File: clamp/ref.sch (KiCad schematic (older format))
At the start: 23 parts, among them P4 CONN_01X06, Q1 2N3904, U12 LTZ1000, U13 LM741, U14 LM741

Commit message: add extra caps, and separate heater gnd return
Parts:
- removed P4: CONN_01X06, Pin_Headers:Pin_Header_Straight_1x06, symbol CONN_01X06
- added C31, C32: C, Capacitors_SMD:C_1206, symbol C
- added P4: CONN_01X08, symbol CONN_01X08
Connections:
- net +VE: now also C31.1, P4.1 (P1)
- net -VE: now also C32.1, P4.3 (P3)
- net GND: now also C31.2, C32.2, P4.2 (P2), P4.6 (P6), P4.7 (P7), P4.8 (P8); no longer D8.2 (C)
- net REF: now also P4.4 (P4)
- new net GND-H: D8.2 (C), P4.5 (P5)
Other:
- moved on the sheet: C27, C28, C33, C34
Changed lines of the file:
@@
 REF
 Connection ~ 9250 2250
-$Comp
-L CONN_01X06 P4
-U 1 1 58643775
-P 2900 1300
-F 0 "P4" H 2900 1650 50  0000 C CNN
-F 1 "CONN_01X06" V 3000 1300 50  0000 C CNN
-F 2 "Pin_Headers:Pin_Header_Straight_1x06" H 2900 1300 50  0001 C CNN
-F 3 "" H 2900 1300 50  0000 C CNN
-	1    2900 1300
-	-1   0    0    -1
-$EndComp
-Text GLabel 3100 1050 2    60   Input ~ 0
+Text GLabel 2850 900  2    60   Input ~ 0
 +VE
-Text GLabel 3100 1250 2    60   Input ~ 0
+Text GLabel 2850 1100 2    60   Input ~ 0
 -VE
-Text GLabel 3100 1150 2    60   Input ~ 0
-GND
-Text GLabel 3100 1350 2    60   Input ~ 0
+Text GLabel 2850 1000 2    60   Input ~ 0
+GND
+Text GLabel 2850 1200 2    60   Input ~ 0
 REF
-Text GLabel 3100 1450 2    60   Input ~ 0
-GND
-Text GLabel 3100 1550 2    60   Input ~ 0
+Text GLabel 2850 1600 2    60   Input ~ 0
+GND
+Text GLabel 2850 1400 2    60   Input ~ 0
 GND
 NoConn ~ 8350 3450
@@
 L C C27
 U 1 1 586449E6
-P 6550 1100
-F 0 "C27" H 6575 1200 50  0000 L CNN
-F 1 "C" H 6575 1000 50  0000 L CNN
-F 2 "Capacitors_SMD:C_1206" H 6588 950 50  0001 C CNN
-F 3 "" H 6550 1100 50  0000 C CNN
-	1    6550 1100
-	1    0    0    -1
-$EndComp
-Text GLabel 6350 850  1    60   Input ~ 0
+P 4700 1100
+F 0 "C27" H 4725 1200 50  0000 L CNN
+F 1 "C" H 4725 1000 50  0000 L CNN
+F 2 "Capacitors_SMD:C_1206" H 4738 950 50  0001 C CNN
+F 3 "" H 4700 1100 50  0000 C CNN
+	1    4700 1100
+	1    0    0    -1
+$EndComp
+Text GLabel 4500 850  1    60   Input ~ 0
 +VE
 Wire Wire Line
-	6350 850  6350 950
-Wire Wire Line
-	6350 950  6800 950
-Connection ~ 6550 950
-Text GLabel 6550 1250 3    60   Input ~ 0
+	4500 850  4500 950
+Wire Wire Line
+	4500 950  5200 950
+Connection ~ 4700 950
+Text GLabel 4700 1250 3    60   Input ~ 0
 GND
 $Comp
 L C C28
 U 1 1 586449F9
-P 6800 1100
-F 0 "C28" H 6825 1200 50  0000 L CNN
-F 1 "C" H 6825 1000 50  0000 L CNN
-F 2 "Capacitors_SMD:C_1206" H 6838 950 50  0001 C CNN
-F 3 "" H 6800 1100 50  0000 C CNN
-	1    6800 1100
-	1    0    0    -1
-$EndComp
-Connection ~ 6800 950
-Text GLabel 6800 1250 3    60   Input ~ 0
+P 4950 1100
+F 0 "C28" H 4975 1200 50  0000 L CNN
+F 1 "C" H 4975 1000 50  0000 L CNN
+F 2 "Capacitors_SMD:C_1206" H 4988 950 50  0001 C CNN
+F 3 "" H 4950 1100 50  0000 C CNN
+	1    4950 1100
+	1    0    0    -1
+$EndComp
+Connection ~ 4950 950
+Text GLabel 4950 1250 3    60   Input ~ 0
 GND
 $Comp
 L C C33
 U 1 1 58644A04
-P 8500 1100
-F 0 "C33" H 8525 1200 50  0000 L CNN
-F 1 "C" H 8525 1000 50  0000 L CNN
-F 2 "Capacitors_SMD:C_1206" H 8538 950 50  0001 C CNN
-F 3 "" H 8500 1100 50  0000 C CNN
-	1    8500 1100
-	1    0    0    -1
-$EndComp
-Wire Wire Line
-	8300 850  8300 950
-Wire Wire Line
-	8300 950  8750 950
-Connection ~ 8500 950
-Text GLabel 8500 1250 3    60   Input ~ 0
+P 6650 1100
+F 0 "C33" H 6675 1200 50  0000 L CNN
+F 1 "C" H 6675 1000 50  0000 L CNN
+F 2 "Capacitors_SMD:C_1206" H 6688 950 50  0001 C CNN
+F 3 "" H 6650 1100 50  0000 C CNN
+	1    6650 1100
+	1    0    0    -1
+$EndComp
+Wire Wire Line
+	6450 850  6450 950
+Wire Wire Line
+	6450 950  7150 950
+Connection ~ 6650 950
+Text GLabel 6650 1250 3    60   Input ~ 0
 GND
 $Comp
 L C C34
 U 1 1 58644A16
-P 8750 1100
-F 0 "C34" H 8775 1200 50  0000 L CNN
-F 1 "C" H 8775 1000 50  0000 L CNN
-F 2 "Capacitors_SMD:C_1206" H 8788 950 50  0001 C CNN
-F 3 "" H 8750 1100 50  0000 C CNN
-	1    8750 1100
-	1    0    0    -1
-$EndComp
-Connection ~ 8750 950
-Text GLabel 8750 1250 3    60   Input ~ 0
-GND
-Text GLabel 8300 850  1    60   Input ~ 0
+P 6900 1100
+F 0 "C34" H 6925 1200 50  0000 L CNN
+F 1 "C" H 6925 1000 50  0000 L CNN
+F 2 "Capacitors_SMD:C_1206" H 6938 950 50  0001 C CNN
+F 3 "" H 6900 1100 50  0000 C CNN
+	1    6900 1100
+	1    0    0    -1
+$EndComp
+Connection ~ 6900 950
+Text GLabel 6900 1250 3    60   Input ~ 0
+GND
+Text GLabel 6450 850  1    60   Input ~ 0
 -VE
 Wire Wire Line
@@
 Connection ~ 4300 4200
 Wire Wire Line
-	5050 3750 5050 4200
-Connection ~ 5050 4200
+	5050 3750 5050 4450
+Text GLabel 5050 4450 3    60   Input ~ 0
+GND-H
+Text GLabel 2850 1300 2    60   Input ~ 0
+GND-H
+$Comp
+L CONN_01X08 P4
+U 1 1 586C60C9
+P 2650 1250
+F 0 "P4" H 2650 1700 50  0000 C CNN
+F 1 "CONN_01X08" V 2750 1250 50  0000 C CNN
+F 2 "" H 2650 1250 50  0000 C CNN
+F 3 "" H 2650 1250 50  0000 C CNN
+	1    2650 1250
+	-1   0    0    -1
+$EndComp
+Text GLabel 2850 1500 2    60   Input ~ 0
+GND
+$Comp
+L C C31
+U 1 1 586C63F8
+P 5200 1100
+F 0 "C31" H 5225 1200 50  0000 L CNN
+F 1 "C" H 5225 1000 50  0000 L CNN
+F 2 "Capacitors_SMD:C_1206" H 5238 950 50  0001 C CNN
+F 3 "" H 5200 1100 50  0000 C CNN
+	1    5200 1100
+	1    0    0    -1
+$EndComp
+Text GLabel 5200 1250 3    60   Input ~ 0
+GND
+$Comp
+L C C32
+U 1 1 586C6539
+P 7150 1100
+F 0 "C32" H 7175 1200 50  0000 L CNN
+F 1 "C" H 7175 1000 50  0000 L CNN
+F 2 "Capacitors_SMD:C_1206" H 7188 950 50  0001 C CNN
+F 3 "" H 7150 1100 50  0000 C CNN
+	1    7150 1100
+	1    0    0    -1
+$EndComp
+Text GLabel 7150 1250 3    60   Input ~ 0
+GND
 $EndSCHEMATC

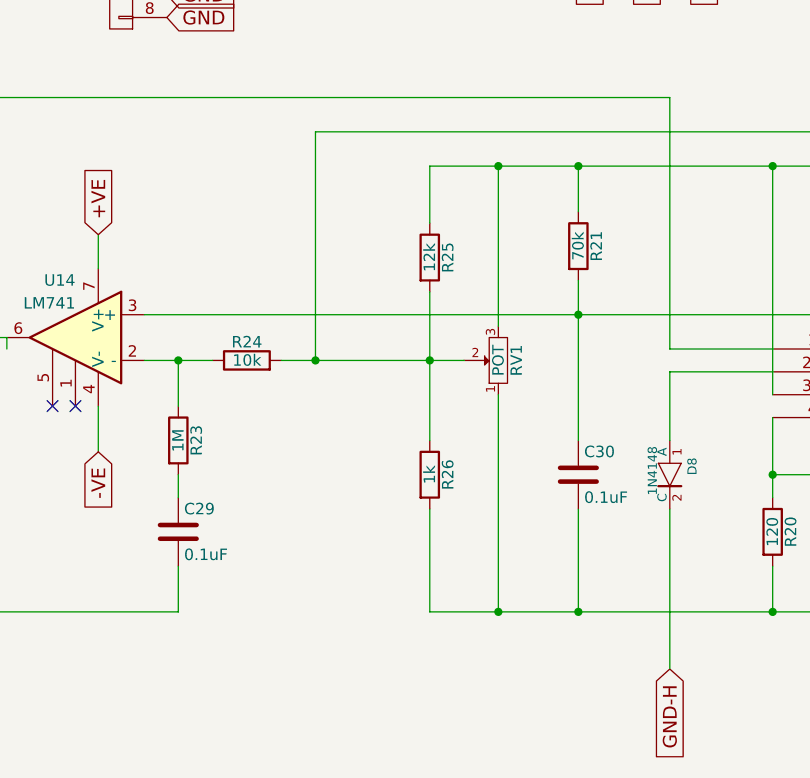
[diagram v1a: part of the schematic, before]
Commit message: remove trimpot add extra resitor
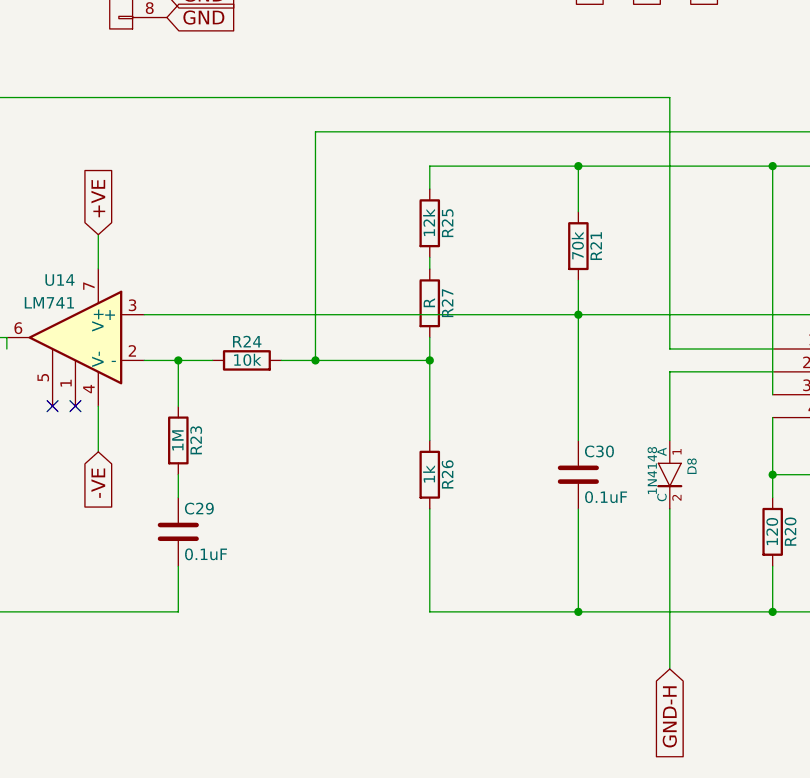
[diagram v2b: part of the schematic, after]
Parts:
- removed RV1: POT, Potentiometers:Potentiometer_Bourns_3296Y_3-8Zoll_Angular_ScrewUp, symbol POT
- added R27: R, symbol R
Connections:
- net at R24.2, R26.1, U12.6 (B2): now also R27.2; no longer R25.2
- new net: R25.2, R27.1
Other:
- moved on the sheet: R25
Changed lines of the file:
@@
 	-1   0    0    -1
 $EndComp
-$Comp
-L POT RV1
-U 1 1 5864A545
-P 4300 3100
-F 0 "RV1" H 4300 3020 50  0000 C CNN
-F 1 "POT" H 4300 3100 50  0000 C CNN
-F 2 "Potentiometers:Potentiometer_Bourns_3296Y_3-8Zoll_Angular_ScrewUp" H 4300 3100 50  0001 C CNN
-F 3 "" H 4300 3100 50  0000 C CNN
-	1    4300 3100
-	0    -1   -1   0
-$EndComp
 Connection ~ 5500 2250
 Wire Wire Line
 	2750 2900 6600 2900
-Wire Wire Line
-	4300 2250 4300 2950
-Wire Wire Line
-	4300 3250 4300 4200
 Connection ~ 5500 4200
 Wire Wire Line
@@
 	2750 3100 3050 3100
 Wire Wire Line
-	3350 3100 4150 3100
+	3350 3100 4000 3100
 Wire Wire Line
 	5050 3150 5500 3150
@@
 L R R25
 U 1 1 5865B477
-P 4000 2650
-F 0 "R25" V 4080 2650 50  0000 C CNN
-F 1 "12k" V 4000 2650 50  0000 C CNN
-F 2 "Resistors_ThroughHole:Resistor_TO-220_Vertical" V 3930 2650 50  0001 C CNN
-F 3 "" H 4000 2650 50  0000 C CNN
-	1    4000 2650
+P 4000 2500
+F 0 "R25" V 4080 2500 50  0000 C CNN
+F 1 "12k" V 4000 2500 50  0000 C CNN
+F 2 "Resistors_ThroughHole:Resistor_TO-220_Vertical" V 3930 2500 50  0001 C CNN
+F 3 "" H 4000 2500 50  0000 C CNN
+	1    4000 2500
 	1    0    0    -1
 $EndComp
@@
 $EndComp
 Wire Wire Line
-	4000 2250 4000 2500
-Connection ~ 4300 2250
-Wire Wire Line
-	4000 2800 4000 3450
+	4000 3000 4000 3450
 Connection ~ 4000 3100
 Wire Wire Line
 	4000 3750 4000 4200
-Connection ~ 4300 4200
 Wire Wire Line
 	5050 3750 5050 4450
@@
 Text GLabel 7150 1250 3    60   Input ~ 0
 GND
+$Comp
+L R R27
+U 1 1 586C6B33
+P 4000 2850
+F 0 "R27" V 4080 2850 50  0000 C CNN
+F 1 "R" V 4000 2850 50  0000 C CNN
+F 2 "" V 3930 2850 50  0000 C CNN
+F 3 "" H 4000 2850 50  0000 C CNN
+	1    4000 2850
+	1    0    0    -1
+$EndComp
+Wire Wire Line
+	4000 2650 4000 2700
+Wire Wire Line
+	4000 2250 4000 2350
 $EndSCHEMATC

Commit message: update
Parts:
- added R28: 0, symbol R
- C27, C33: value C -> 10uF
- C28, C31, C32, C34: value C -> 0.1uF
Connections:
- net GND: now also R28.1
- net GND-H: now also R28.2
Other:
- moved on the sheet: C26, R20, r1
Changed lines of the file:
@@
 L R R20
 U 1 1 58642F48
-P 5500 3850
-F 0 "R20" V 5580 3850 50  0000 C CNN
-F 1 "120" V 5500 3850 50  0000 C CNN
-F 2 "Resistors_ThroughHole:Resistor_TO-220_Vertical" V 5430 3850 50  0001 C CNN
-F 3 "" H 5500 3850 50  0000 C CNN
-	1    5500 3850
-	1    0    0    -1
-$EndComp
-Wire Wire Line
-	5500 3350 5500 3700
+P 5500 3900
+F 0 "R20" V 5580 3900 50  0000 C CNN
+F 1 "120" V 5500 3900 50  0000 C CNN
+F 2 "Resistors_ThroughHole:Resistor_TO-220_Vertical" V 5430 3900 50  0001 C CNN
+F 3 "" H 5500 3900 50  0000 C CNN
+	1    5500 3900
+	1    0    0    -1
+$EndComp
+Wire Wire Line
+	5500 3350 5500 3750
 $Comp
 L R r1
 U 1 1 5864309C
-P 7400 2600
-F 0 "r1" V 7480 2600 50  0000 C CNN
-F 1 "70k" V 7400 2600 50  0000 C CNN
-F 2 "Resistors_ThroughHole:Resistor_TO-220_Vertical" V 7330 2600 50  0001 C CNN
-F 3 "" H 7400 2600 50  0000 C CNN
-	1    7400 2600
-	1    0    0    -1
-$EndComp
-Wire Wire Line
-	7400 2250 7400 2450
+P 7400 2650
+F 0 "r1" V 7480 2650 50  0000 C CNN
+F 1 "70k" V 7400 2650 50  0000 C CNN
+F 2 "Resistors_ThroughHole:Resistor_TO-220_Vertical" V 7330 2650 50  0001 C CNN
+F 3 "" H 7400 2650 50  0000 C CNN
+	1    7400 2650
+	1    0    0    -1
+$EndComp
+Wire Wire Line
+	7400 2250 7400 2500
 Connection ~ 7400 2250
 Wire Wire Line
-	7400 2750 7400 3700
+	7400 2800 7400 3750
 Wire Wire Line
 	6500 3250 6800 3250
@@
 Connection ~ 5500 3600
 Wire Wire Line
-	5500 4200 5500 4000
+	5500 4200 5500 4050
 $Comp
 L C C26
 U 1 1 58643272
-P 7400 3850
-F 0 "C26" H 7425 3950 50  0000 L CNN
-F 1 "22nF" H 7425 3750 50  0000 L CNN
-F 2 "Capacitors_SMD:C_1206" H 7438 3700 50  0001 C CNN
-F 3 "" H 7400 3850 50  0000 C CNN
-	1    7400 3850
-	1    0    0    -1
-$EndComp
-Wire Wire Line
-	7400 4000 7400 4450
+P 7400 3900
+F 0 "C26" H 7425 4000 50  0000 L CNN
+F 1 "22nF" H 7425 3800 50  0000 L CNN
+F 2 "Capacitors_SMD:C_1206" H 7438 3750 50  0001 C CNN
+F 3 "" H 7400 3900 50  0000 C CNN
+	1    7400 3900
+	1    0    0    -1
+$EndComp
+Wire Wire Line
+	7400 4050 7400 4450
 Connection ~ 7400 4200
 Wire Wire Line
@@
 P 4700 1100
 F 0 "C27" H 4725 1200 50  0000 L CNN
-F 1 "C" H 4725 1000 50  0000 L CNN
+F 1 "10uF" H 4725 1000 50  0000 L CNN
 F 2 "Capacitors_SMD:C_1206" H 4738 950 50  0001 C CNN
 F 3 "" H 4700 1100 50  0000 C CNN
@@
 P 4950 1100
 F 0 "C28" H 4975 1200 50  0000 L CNN
-F 1 "C" H 4975 1000 50  0000 L CNN
+F 1 "0.1uF" H 4975 1000 50  0000 L CNN
 F 2 "Capacitors_SMD:C_1206" H 4988 950 50  0001 C CNN
 F 3 "" H 4950 1100 50  0000 C CNN
@@
 P 6650 1100
 F 0 "C33" H 6675 1200 50  0000 L CNN
-F 1 "C" H 6675 1000 50  0000 L CNN
+F 1 "10uF" H 6675 1000 50  0000 L CNN
 F 2 "Capacitors_SMD:C_1206" H 6688 950 50  0001 C CNN
 F 3 "" H 6650 1100 50  0000 C CNN
@@
 P 6900 1100
 F 0 "C34" H 6925 1200 50  0000 L CNN
-F 1 "C" H 6925 1000 50  0000 L CNN
+F 1 "0.1uF" H 6925 1000 50  0000 L CNN
 F 2 "Capacitors_SMD:C_1206" H 6938 950 50  0001 C CNN
 F 3 "" H 6900 1100 50  0000 C CNN
@@
 P 5200 1100
 F 0 "C31" H 5225 1200 50  0000 L CNN
-F 1 "C" H 5225 1000 50  0000 L CNN
+F 1 "0.1uF" H 5225 1000 50  0000 L CNN
 F 2 "Capacitors_SMD:C_1206" H 5238 950 50  0001 C CNN
 F 3 "" H 5200 1100 50  0000 C CNN
@@
 P 7150 1100
 F 0 "C32" H 7175 1200 50  0000 L CNN
-F 1 "C" H 7175 1000 50  0000 L CNN
+F 1 "0.1uF" H 7175 1000 50  0000 L CNN
 F 2 "Capacitors_SMD:C_1206" H 7188 950 50  0001 C CNN
 F 3 "" H 7150 1100 50  0000 C CNN
@@
 Wire Wire Line
 	4000 2250 4000 2350
+Text GLabel 8350 1150 0    60   Input ~ 0
+GND-H
+Text GLabel 9150 1150 2    60   Input ~ 0
+GND
+$Comp
+L R R28
+U 1 1 587DAF89
+P 8700 1150
+F 0 "R28" V 8780 1150 50  0000 C CNN
+F 1 "0" V 8700 1150 50  0000 C CNN
+F 2 "" V 8630 1150 50  0000 C CNN
+F 3 "" H 8700 1150 50  0000 C CNN
+	1    8700 1150
+	0    1    1    0
+$EndComp
+Wire Wire Line
+	8350 1150 8550 1150
+Wire Wire Line
+	8850 1150 9150 1150
 $EndSCHEMATC

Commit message: update
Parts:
- removed R27: R, symbol R
- P4: footprint (none) -> Pin_Headers:Pin_Header_Straight_1x08
- R28: footprint (none) -> Resistors_SMD:R_1206
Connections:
- net at R24.2, R26.1, U12.6 (B2): now also R25.2
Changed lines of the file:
@@
 	9050 3150 9250 3150
 Wire Wire Line
-	9250 3150 9250 2250
+	9250 2250 9250 3150
 Wire Wire Line
 	5500 2250 5500 3250
@@
 	6500 3250 6800 3250
 Wire Wire Line
-	6800 3250 6800 4200
+	6800 4200 6800 3250
 Connection ~ 6800 4200
 Connection ~ 7400 3050
@@
 $EndComp
 Wire Wire Line
-	4000 3000 4000 3450
+	4000 2650 4000 3450
 Connection ~ 4000 3100
 Wire Wire Line
@@
 F 0 "P4" H 2650 1700 50  0000 C CNN
 F 1 "CONN_01X08" V 2750 1250 50  0000 C CNN
-F 2 "" H 2650 1250 50  0000 C CNN
+F 2 "Pin_Headers:Pin_Header_Straight_1x08" H 2650 1250 50  0001 C CNN
 F 3 "" H 2650 1250 50  0000 C CNN
 	1    2650 1250
@@
 Text GLabel 7150 1250 3    60   Input ~ 0
 GND
-$Comp
-L R R27
-U 1 1 586C6B33
-P 4000 2850
-F 0 "R27" V 4080 2850 50  0000 C CNN
-F 1 "R" V 4000 2850 50  0000 C CNN
-F 2 "" V 3930 2850 50  0000 C CNN
-F 3 "" H 4000 2850 50  0000 C CNN
-	1    4000 2850
-	1    0    0    -1
-$EndComp
-Wire Wire Line
-	4000 2650 4000 2700
 Wire Wire Line
 	4000 2250 4000 2350
@@
 F 0 "R28" V 8780 1150 50  0000 C CNN
 F 1 "0" V 8700 1150 50  0000 C CNN
-F 2 "" V 8630 1150 50  0000 C CNN
+F 2 "Resistors_SMD:R_1206" V 8630 1150 50  0001 C CNN
 F 3 "" H 8700 1150 50  0000 C CNN
 	1    8700 1150
